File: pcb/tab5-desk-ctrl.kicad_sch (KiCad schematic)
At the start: 18 parts, among them U1A Socket 1x15 2.54mm, U1B Socket 1x15 2.54mm

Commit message: The companion's carrier board rev2: pins 5 and 6 the way the box uses them, the divider on pin 5 where it sends and the 220R on pin 6 where it listens, as the published tables have it; the DevKit 10 mm further from the jack, and in the room that frees the 5 V input with a 1000 uF electrolytic for the radio's start-up surge, which browned rev1 out on desk power alone; thermal reliefs on the ground pads, with the router keeping other nets off the jack's pin 7; the jack's pin numbers and what each carries on the back; the README, the wiring figure and the companion's defaults to match
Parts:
- added C3: 1000uF 6.3V, Capacitor_THT:CP_Radial_D8.0mm_P3.50mm, symbol Device:C_Polarized
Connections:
- net +5V: now also C3.1
- net DESK_RX: now also RJ45_1.6; no longer RJ45_1.5
- net DESK_TX: now also RJ45_1.5; no longer RJ45_1.6
- net GND: now also C3.2
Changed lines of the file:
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@@
   (title_block
     (title "FlexiSpot / LoctekMotion BLE desk companion")
-    (rev "rev1")
+    (rev "rev2")
     (company "Wouter ten Brinke")
     (comment 1 "ESP32 DevKit V1 30-pin carrier, RJ45 to the control box")
@@
     (stroke (width 0.0))
   )
+  (wire (pts (xy 109.22 39.37) (xy 109.22 41.91))
+    (stroke (width 0.0))
+  )
+  (wire (pts (xy 109.22 49.53) (xy 109.22 52.07))
+    (stroke (width 0.0))
+  )
   (wire (pts (xy 109.22 83.82) (xy 119.38 83.82))
     (stroke (width 0.0))
@@
     (effects (font (size 1.27 1.27)))
   )
-  (global_label "DESK_TX" (shape input) (at 72.39 50.8 0)
-    (effects (font (size 1.27 1.27)))
-  )
-  (global_label "DESK_RX" (shape input) (at 72.39 53.34 0)
+  (global_label "DESK_TX" (shape input) (at 72.39 53.34 0)
+    (effects (font (size 1.27 1.27)))
+  )
+  (global_label "DESK_RX" (shape input) (at 72.39 50.8 0)
     (effects (font (size 1.27 1.27)))
   )
@@
     )
   )
+  (symbol (lib_id "Device:C_Polarized") (at 109.22 45.72 0) (unit 1)
+    (in_bom yes) (on_board yes)
+    (property "Reference" "C3" (at 119.38 44.449999999999996 0)
+      (effects (font (size 1.27 1.27)))
+    )
+    (property "Value" "1000uF 6.3V" (at 119.38 49.53 0)
+      (effects (font (size 1.27 1.27)))
+    )
+    (property "Footprint" "Capacitor_THT:CP_Radial_D8.0mm_P3.50mm" (at 109.22 45.72 0)
+      (effects (font (size 1.27 1.27)) hide)
+    )
+    (property "Datasheet" "~" (at 109.22 45.72 0)
+      (effects (font (size 1.27 1.27)) hide)
+    )
+  )
   (symbol (lib_id "Device:R") (at 123.19 83.82 90) (unit 1)
     (in_bom yes) (on_board yes)
@@
     )
     (property "Datasheet" "~" (at 144.78 110.49 0)
+      (effects (font (size 1.27 1.27)) hide)
+    )
+  )
+  (symbol (lib_id "power:+5V") (at 109.22 39.37 0) (unit 1)
+    (in_bom no) (on_board yes)
+    (property "Reference" "#PWR07" (at 114.3 36.83 0)
+      (effects (font (size 1.27 1.27)) hide)
+    )
+    (property "Value" "+5V" (at 114.3 41.91 0)
+      (effects (font (size 1.27 1.27)) hide)
+    )
+    (property "Footprint" "" (at 109.22 39.37 0)
+      (effects (font (size 1.27 1.27)) hide)
+    )
+    (property "Datasheet" "~" (at 109.22 39.37 0)
+      (effects (font (size 1.27 1.27)) hide)
+    )
+  )
+  (symbol (lib_id "tab5-desk-ctrl:GND_EARTH") (at 109.22 52.07 0) (unit 1)
+    (in_bom no) (on_board yes)
+    (property "Reference" "#PWR11" (at 114.3 49.53 0)
+      (effects (font (size 1.27 1.27)) hide)
+    )
+    (property "Value" "GND" (at 114.3 54.61 0)
+      (effects (font (size 1.27 1.27)) hide)
+    )
+    (property "Footprint" "" (at 109.22 52.07 0)
+      (effects (font (size 1.27 1.27)) hide)
+    )
+    (property "Datasheet" "~" (at 109.22 52.07 0)
       (effects (font (size 1.27 1.27)) hide)
     )
@@
   )
   (symbol_instances
-    (path "/047a4a2f-19f1-442f-b49e-be08b579a171"
+    (path "/38a7c0d5-ddef-495b-b5be-73ec42efd360"
       (reference "RJ45_1") (unit 1) (value "RJ45 8P8C 2xLED") (footprint "Connector_RJ:RJ45_Connfly_DS1128-09-S8xx-S_Horizontal")
     )
-    (path "/bb8bdb76-8b04-489c-9171-2040bc6570a9"
+    (path "/93a86a2a-cd90-45ae-b5f3-32e7c73715a1"
       (reference "R5") (unit 1) (value "220R") (footprint "Resistor_SMD:R_0805_2012Metric")
     )
-    (path "/e1609176-baf5-44c7-80fa-160e1e69f3a4"
+    (path "/0a554116-c610-4cb9-9b84-423f01257ff1"
       (reference "R6") (unit 1) (value "220R") (footprint "Resistor_SMD:R_0805_2012Metric")
     )
-    (path "/41c4639a-fc16-41f0-b319-40b693cbd270"
+    (path "/909dad37-9d7c-4a33-afa1-2f419c203440"
       (reference "F1") (unit 1) (value "PTC 500mA") (footprint "Resistor_SMD:R_1206_3216Metric")
     )
-    (path "/a30a9969-845f-41a9-8392-8e98001c698e"
+    (path "/c939d8d0-161b-48fa-923c-d633606859dc"
       (reference "D1") (unit 1) (value "SS14") (footprint "Diode_SMD:D_SMA")
     )
-    (path "/164b3aac-11e8-48ed-a7e8-a9d4779661b9"
+    (path "/dc382c91-99b3-4416-91be-17df99da45da"
       (reference "C1") (unit 1) (value "22uF 25V") (footprint "Capacitor_SMD:C_1206_3216Metric")
     )
-    (path "/7b6b9f6a-2333-452f-b779-dab2c4d0581c"
+    (path "/a0ae77c6-3c10-400f-a959-bb81267ad3db"
       (reference "C2") (unit 1) (value "100nF 50V") (footprint "Capacitor_SMD:C_0805_2012Metric")
     )
-    (path "/8d91bc16-09ce-45dc-b0c9-07bd10d34e08"
+    (path "/803911d9-4ad0-4342-af9e-39104b503425"
+      (reference "C3") (unit 1) (value "1000uF 6.3V") (footprint "Capacitor_THT:CP_Radial_D8.0mm_P3.50mm")
+    )
+    (path "/7f63c94c-7d7a-40b3-91dd-16b64cba7c5d"
       (reference "R1") (unit 1) (value "10k") (footprint "Resistor_SMD:R_0805_2012Metric")
     )
-    (path "/8f33378a-f863-4d27-b3cf-7c8487b7475c"
+    (path "/bb54d2aa-37f4-489c-b72a-abfec8a37cd6"
       (reference "R2") (unit 1) (value "15k") (footprint "Resistor_SMD:R_0805_2012Metric")
     )
-    (path "/bc0ec7a4-82a5-4bf6-8f25-55a9de6457ae"
+    (path "/bd6bc78d-ccfb-4678-a927-f6fb251fbd18"
       (reference "D2") (unit 1) (value "BAT54S") (footprint "Package_TO_SOT_SMD:SOT-23")
     )
-    (path "/6bdd057d-8b80-4c73-9933-86992f385b9a"
+    (path "/3561ce52-8487-4f0c-a31e-55e230d85240"
       (reference "R3") (unit 1) (value "220R") (footprint "Resistor_SMD:R_0805_2012Metric")
     )
-    (path "/f72f1b08-7874-4b86-bb27-b3755f139e1c"
+    (path "/2ec45a0a-d839-4233-87ac-709dc064b3a9"
       (reference "R4") (unit 1) (value "220R") (footprint "Resistor_SMD:R_0805_2012Metric")
     )
-    (path "/dfcf6716-0e85-4ee4-8e7d-db31cbe70ca4"
+    (path "/0e5f4489-fc81-46ad-80f7-71cdaf5f0ddc"
       (reference "U1A") (unit 1) (value "Socket 1x15 2.54mm") (footprint "Connector_PinSocket_2.54mm:PinSocket_1x15_P2.54mm_Vertical")
     )
-    (path "/d1a36b01-9733-4af2-868a-d6aa7ea028e8"
+    (path "/cbf4873d-c21f-4889-bd80-3ab66262f6a3"
       (reference "U1B") (unit 1) (value "Socket 1x15 2.54mm") (footprint "Connector_PinSocket_2.54mm:PinSocket_1x15_P2.54mm_Vertical")
     )
-    (path "/51db79d3-6102-4d0d-a21c-5ca8047782de"
+    (path "/5d6d783b-bd15-495f-84e1-7f48ea18290d"
       (reference "H1") (unit 1) (value "M3") (footprint "MountingHole:MountingHole_3.2mm_M3")
     )
-    (path "/c814aa54-c9d4-4f7e-9ccd-f1304dd1e05d"
+    (path "/34b80dc2-1883-4a11-8eca-f06bcd7da88d"
       (reference "H2") (unit 1) (value "M3") (footprint "MountingHole:MountingHole_3.2mm_M3")
     )
-    (path "/b82ac476-39bb-498c-9683-0e65839e7730"
+    (path "/7377d396-e35e-4caf-8bd0-ad2c7a85980b"
       (reference "H3") (unit 1) (value "M3") (footprint "MountingHole:MountingHole_3.2mm_M3")
     )
-    (path "/00dd6381-b739-4b40-bd2c-e421c5d7a9b8"
+    (path "/fb17426e-e6df-4694-873d-67c46c6b69d8"
       (reference "H4") (unit 1) (value "M3") (footprint "MountingHole:MountingHole_3.2mm_M3")
     )
-    (path "/9d317022-6ac8-440e-9c45-76f77361c9c7"
+    (path "/70191a35-ca1c-431b-a433-1dc1089d43a4"
       (reference "#PWR08") (unit 1) (value "GND") (footprint "")
     )
-    (path "/db7d5754-477f-4b0c-8dd0-ec0c99f3a940"
+    (path "/f8aafd38-856f-4aac-9dd7-66ac46c21c9c"
       (reference "#PWR09") (unit 1) (value "GND") (footprint "")
     )
-    (path "/95241d61-0a2b-495d-9460-f69aa60de6e6"
+    (path "/dbe483e9-a004-4c3c-ab55-911305a54ef2"
       (reference "#PWR10") (unit 1) (value "GND") (footprint "")
     )
-    (path "/a45b00aa-da7e-439e-b44e-e13ddcb86cc5"
+    (path "/b123c2de-2239-4e6c-9b73-9d7a3bef4079"
       (reference "#PWR02") (unit 1) (value "GND") (footprint "")
     )
-    (path "/e746e51e-89e6-40bc-860e-d19e38bfffde"
+    (path "/28bdca3a-c704-49e7-a8ad-82e51ed681f7"
       (reference "#PWR03") (unit 1) (value "GND") (footprint "")
     )
-    (path "/65305762-6136-4a0f-91db-57d11f05fa77"
+    (path "/1d03debb-fc60-41a0-98ad-984704eeb6d2"
       (reference "#PWR04") (unit 1) (value "GND") (footprint "")
     )
-    (path "/71d388e5-249b-492b-afcd-4186787934c4"
+    (path "/f585db8b-2fdf-44a1-b56a-54e9e75f034e"
       (reference "#PWR05") (unit 1) (value "GND") (footprint "")
     )
-    (path "/07a02f51-4ded-423d-8026-15741709542a"
+    (path "/09627045-1143-47ba-a426-770908fb10a4"
+      (reference "#PWR07") (unit 1) (value "+5V") (footprint "")
+    )
+    (path "/58ea4610-1880-47e6-b40b-3538e500ec20"
+      (reference "#PWR11") (unit 1) (value "GND") (footprint "")
+    )
+    (path "/0eb25d1d-046c-4bde-89f5-138bb1cfb49d"
       (reference "#PWR01") (unit 1) (value "+5V") (footprint "")
     )
-    (path "/6849af3d-754b-4106-9f63-4f6640bc323a"
+    (path "/2b64b3fc-6df4-4339-a59b-7dc000f01b0b"
       (reference "#PWR06") (unit 1) (value "+3V3") (footprint "")
     )
-    (path "/07ceab7a-f71b-44b0-8c23-c62d18bfc02f"
+    (path "/84943abe-a030-4052-9685-cfacbcc8aaf6"
       (reference "#FLG01") (unit 1) (value "PWR_FLAG") (footprint "")
     )
-    (path "/b6f37b5e-83fa-45a3-b2f4-c313c7e7284a"
+    (path "/0482f3cc-4ae4-4c3c-9597-9b0129312fbb"
       (reference "#FLG02") (unit 1) (value "PWR_FLAG") (footprint "")
     )
-    (path "/770bf0d1-4f0d-4a97-99ed-73a166fdda60"
+    (path "/a0d37bb1-168b-4ff3-80b4-8e01206195a4"
       (reference "#FLG03") (unit 1) (value "PWR_FLAG") (footprint "")
     )

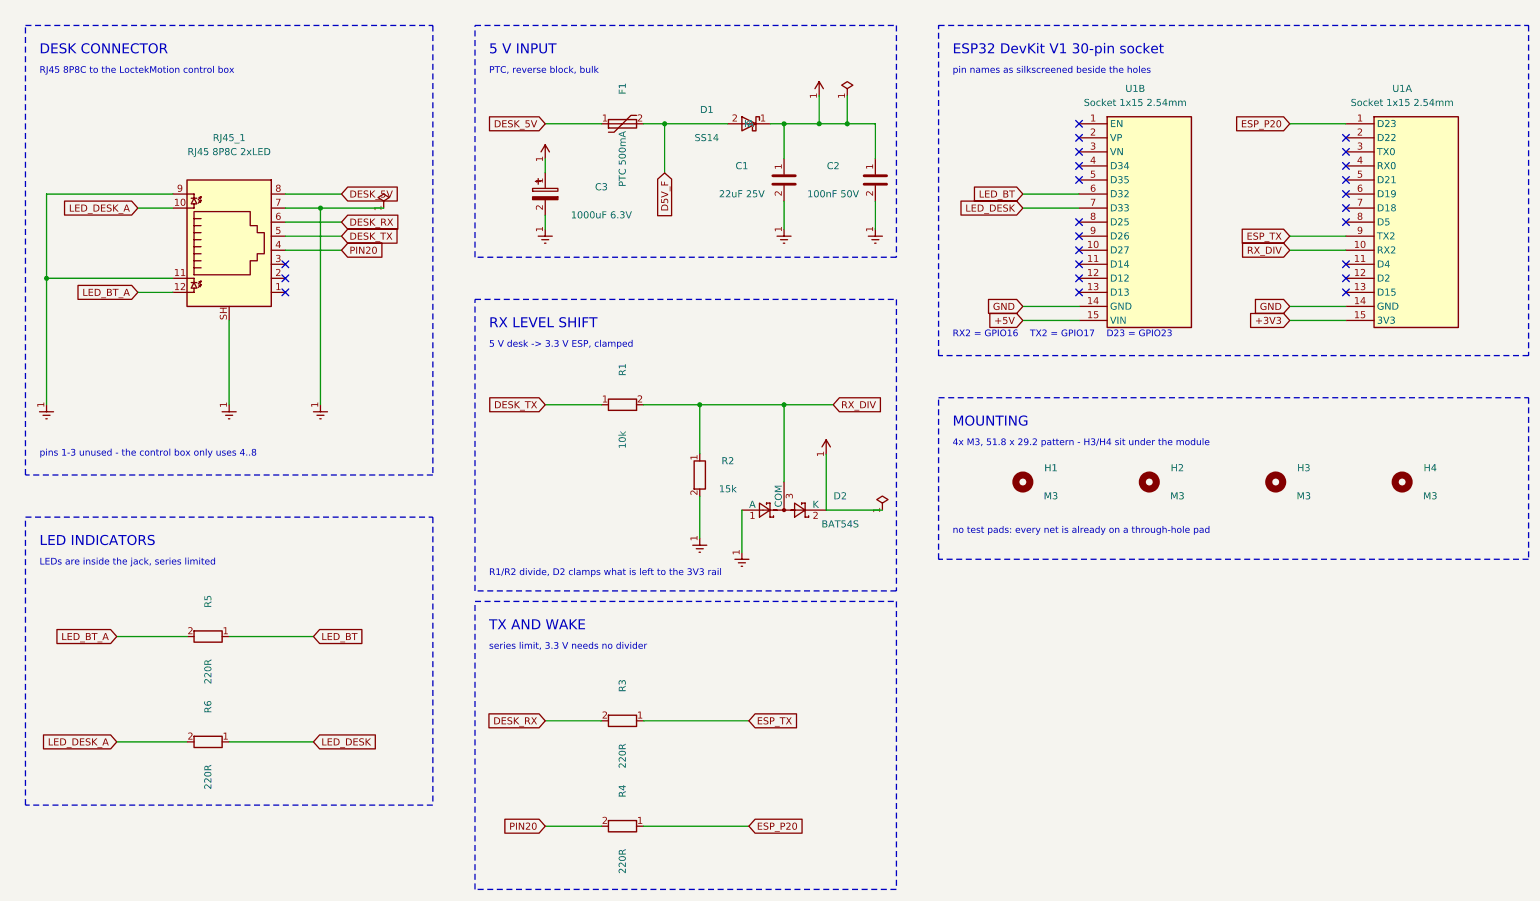
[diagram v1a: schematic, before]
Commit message: The rev2 board 10 mm longer again, so the DevKit stays clear of C3 however far it reaches past its first pin; the DevKit's pin names, BT, LINK and C3's + on the back as well, where the probe goes; the schematic redrawn: left to right from the jack to the module, power as named symbols instead of labels, every field level, no pin numbers on two-pin parts, each label at the end of its stub, C3 in the 5 V input and the new mounting pattern; check_sch.py reads a field's justification and its symbol's turn
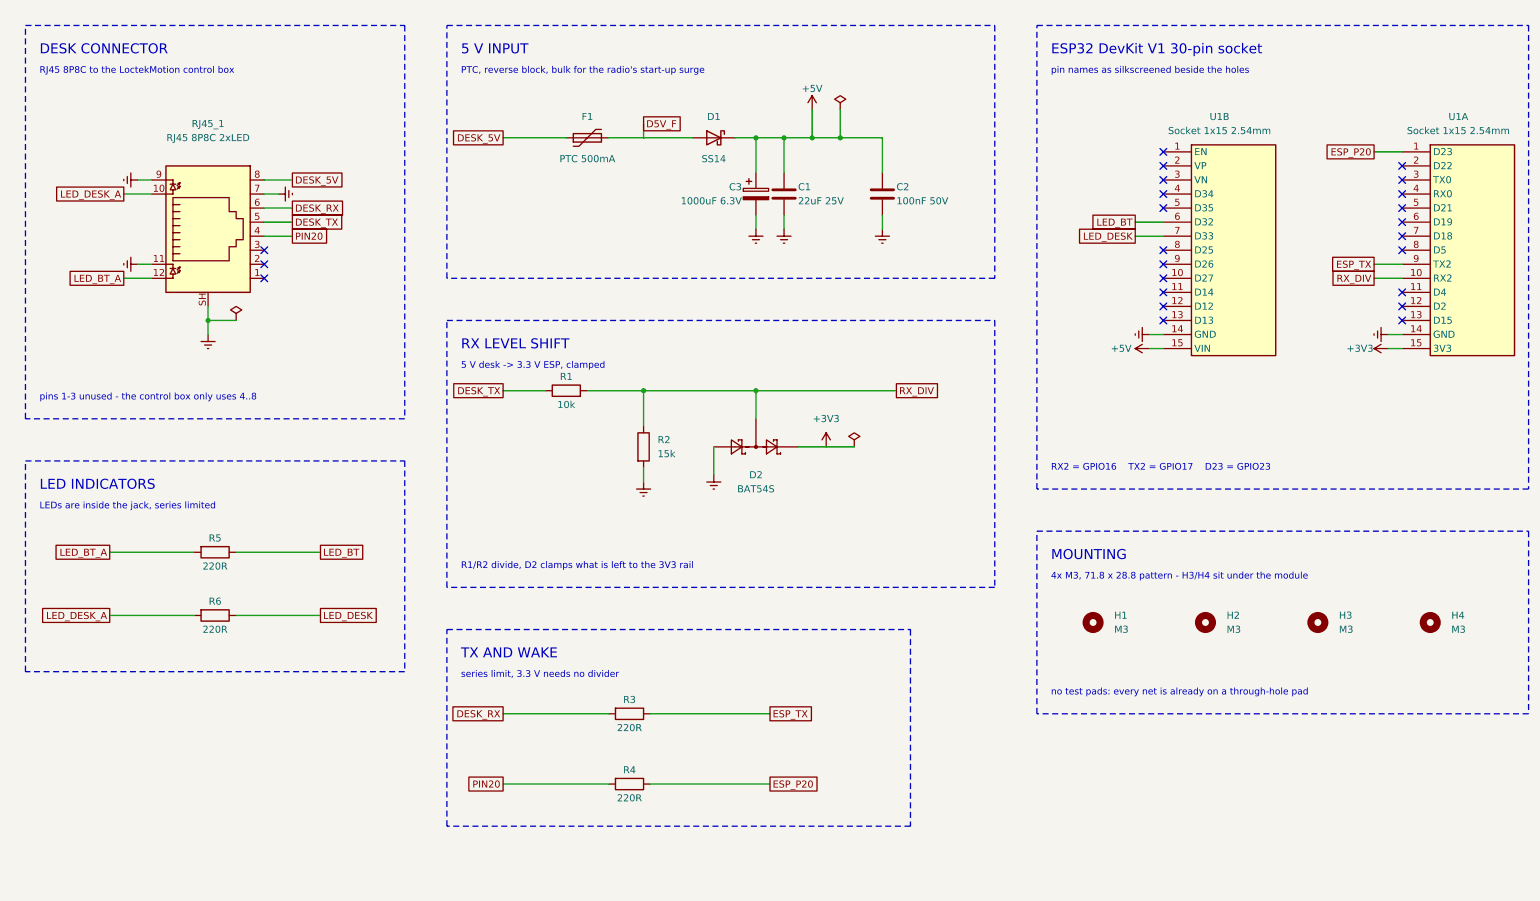
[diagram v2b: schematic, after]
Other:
- note added: "4x M3, 71.8 x 28.8 pattern - H3/H4 sit under the module"
- note added: "PTC, reverse block, bulk for the radio's start-up surge"
- note removed: "4x M3, 51.8 x 29.2 pattern - H3/H4 sit under the module"
- note removed: "PTC, reverse block, bulk"

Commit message: The rev2 schematic on A5 and packed: plain net labels written over their stubs, the board's signal nets named as KiCad names them on the root sheet so parity holds, the LEDs beside the jack, and notes with the box's pinout, the readings to expect at idle, the GPIOs, what the LEDs say and which way C3 goes; LED nets named BT and LINK as on the silkscreen; C3 470 uF 10 V, and optional
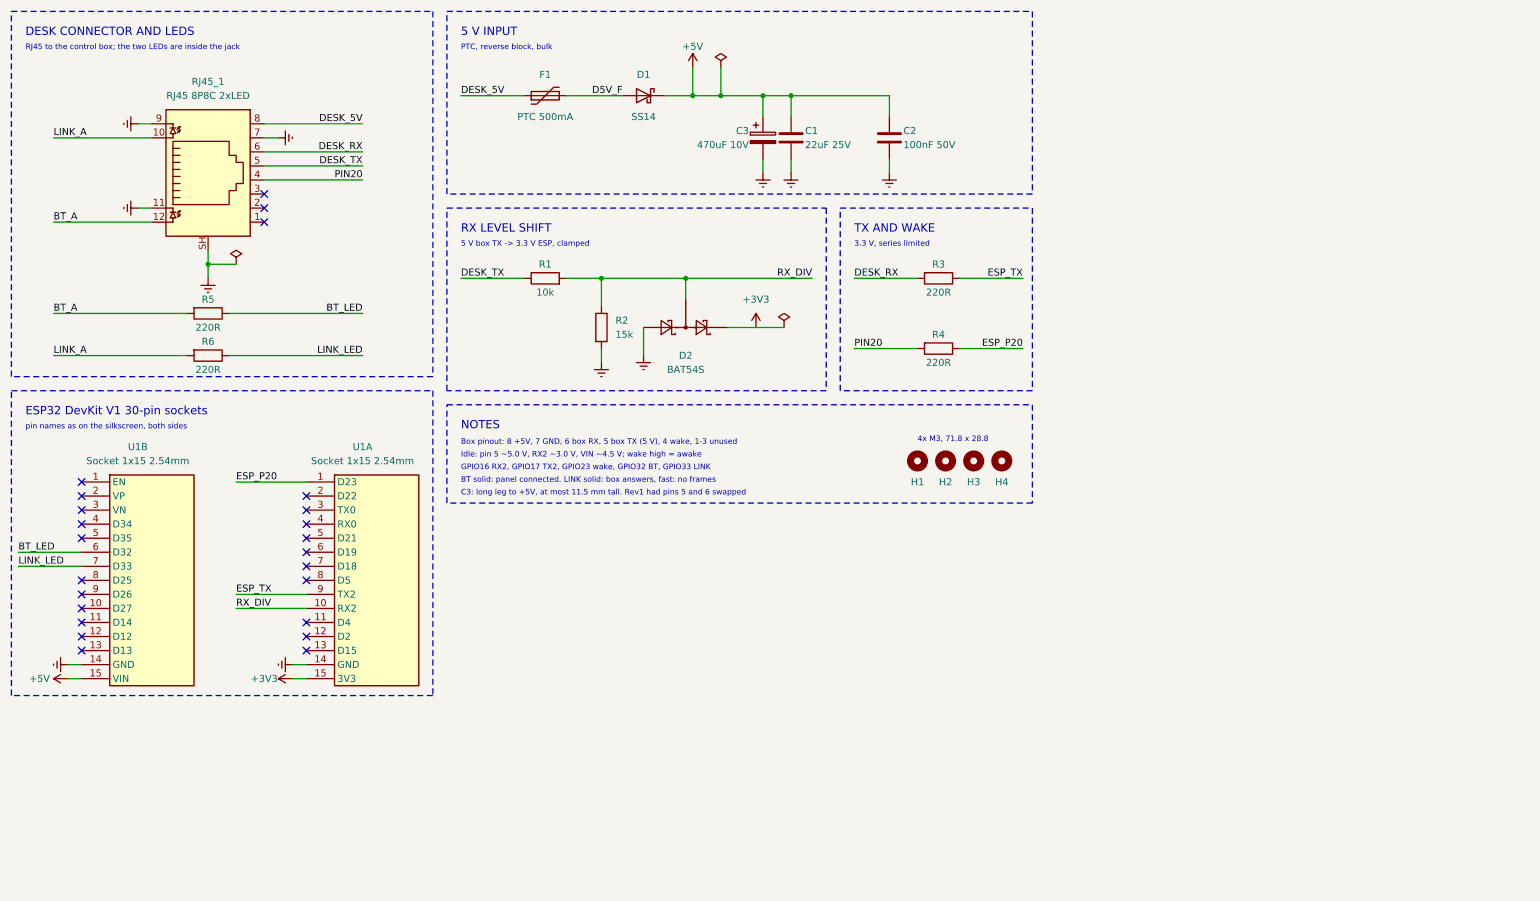
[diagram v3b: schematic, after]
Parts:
- C3: value 1000uF 6.3V -> 470uF 10V
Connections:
- net LED_BT renamed BT_LED
- net LED_BT_A renamed BT_A
- net LED_DESK renamed LINK_LED
- net LED_DESK_A renamed LINK_A
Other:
- note added: "3.3 V, series limited"
- note added: "4x M3, 71.8 x 28.8"
- note added: "5 V box TX -> 3.3 V ESP, clamped"
- note added: "BT solid: panel connected. LINK solid: box answers, fast: no frames"
- note added: "Box pinout: 8 +5V, 7 GND, 6 box RX, 5 box TX (5 V), 4 wake, 1-3 unused"
- note added: "C3: long leg to +5V, at most 11.5 mm tall. Rev1 had pins 5 and 6 swapped"
- note added: "DESK CONNECTOR AND LEDS"
- note added: "ESP32 DevKit V1 30-pin sockets"
- note added: "GPIO16 RX2, GPIO17 TX2, GPIO23 wake, GPIO32 BT, GPIO33 LINK"
- note added: "Idle: pin 5 ~5.0 V, RX2 ~3.0 V, VIN ~4.5 V; wake high = awake"
- note added: "NOTES"
- note added: "PTC, reverse block, bulk"
- note added: "RJ45 to the control box; the two LEDs are inside the jack"
- note added: "pin names as on the silkscreen, both sides"
- note removed: "4x M3, 71.8 x 28.8 pattern - H3/H4 sit under the module"
- note removed: "5 V desk -> 3.3 V ESP, clamped"
- note removed: "DESK CONNECTOR"
- note removed: "ESP32 DevKit V1 30-pin socket"
- note removed: "LED INDICATORS"
- note removed: "LEDs are inside the jack, series limited"
- note removed: "MOUNTING"
- note removed: "PTC, reverse block, bulk for the radio's start-up surge"
- note removed: "R1/R2 divide, D2 clamps what is left to the 3V3 rail"
- note removed: "RJ45 8P8C to the LoctekMotion control box"
- note removed: "RX2 = GPIO16 TX2 = GPIO17 D23 = GPIO23"
- note removed: "no test pads: every net is already on a through-hole pad"
- note removed: "pin names as silkscreened beside the holes"
- note removed: "pins 1-3 unused - the control box only uses 4..8"
- note removed: "series limit, 3.3 V needs no divider"
